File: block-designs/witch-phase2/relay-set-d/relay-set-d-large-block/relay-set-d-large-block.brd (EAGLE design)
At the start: 99.1 x 78.7 mm, 96 parts, among them IC1 74LVC1G06DBV, IC10 741G3157DBVR, IC11 741G3157DBVR, IC12 74LVC1G79DBV, IC13 74LVC1G79DBV, IC14 74LVC1G79DBV, IC15 74LVC1G79DBV, IC16 74LVC1G79DBV, IC17 74LVC1G08DBV, IC18 74LVC1G08DBV, IC19 74LVC1G08DBV, IC2 74LVC1G06DBV, IC20 74LVC1G08DBV, IC21 74LVC1G08DBV, IC22 74LVC1G08DBV, IC23 74LVC1G08DBV, IC24 74LVC1G08DBV, IC25 74LVC1G08DBV, IC26 74LVC1G08DBV, IC27 741G3157DBVR, IC28 741G3157DBVR, IC29 741G3157DBVR, IC3 74LVC1G06DBV, IC30 741G3157DBVR, IC31 741G3157DBVR, IC32 741G3157DBVR, IC33 741G3157DBVR, IC34 741G3157DBVR, IC35 741G3157DBVR, IC36 741G3157DBVR, IC37 74LVC1G32DBV, IC38 74LVC1G32DBV, IC39 74LVC1G32DBV, IC4 74LVC1G06DBV, IC40 74LVC1G32DBV, IC41 74LVC1G32DBV, IC42 74LVC1G32DBV, IC43 74LVC1G32DBV, IC44 74LVC1G32DBV, IC45 74LVC1G06DBV, IC46 74LVC1G06DBV, IC47 74LVC1G06DBV, IC48 74LVC1G06DBV, IC49 74LVC1G06DBV, IC5 74LVC1G06DBV, IC50 74LVC1G06DBV, IC51 74LVC1G06DBV, IC52 74LVC1G06DBV, IC53 74LVC1G06DBV, IC54 74LVC1G06DBV, IC55 74LVC1G06DBV, IC56 74LVC1G06DBV, IC6 741G3157DBVR, IC7 741G3157DBVR, IC8 741G3157DBVR, IC9 741G3157DBVR, Q1 MMBT2907ALT1SMD, Q2 MMBT2907ALT1SMD

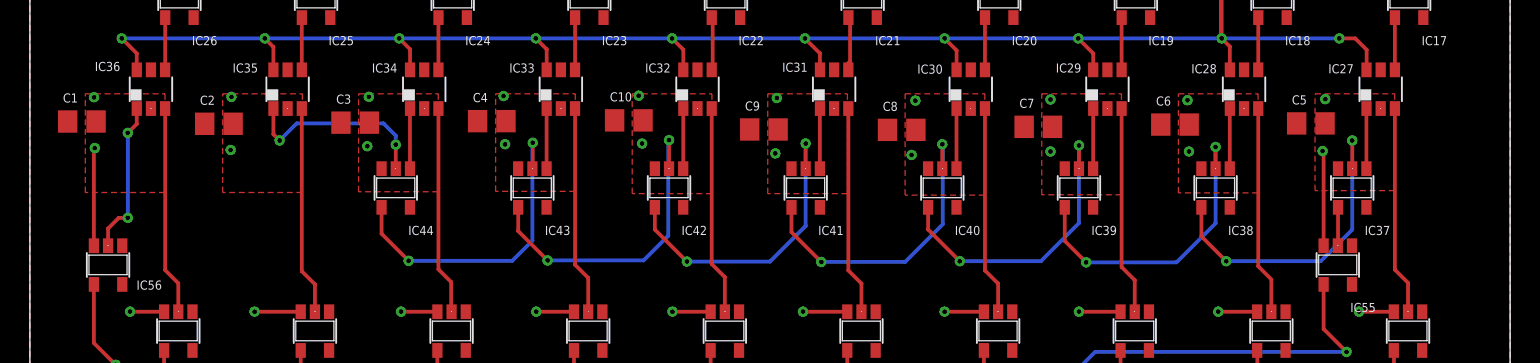
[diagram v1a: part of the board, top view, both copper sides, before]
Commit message: add pull down resistors to design
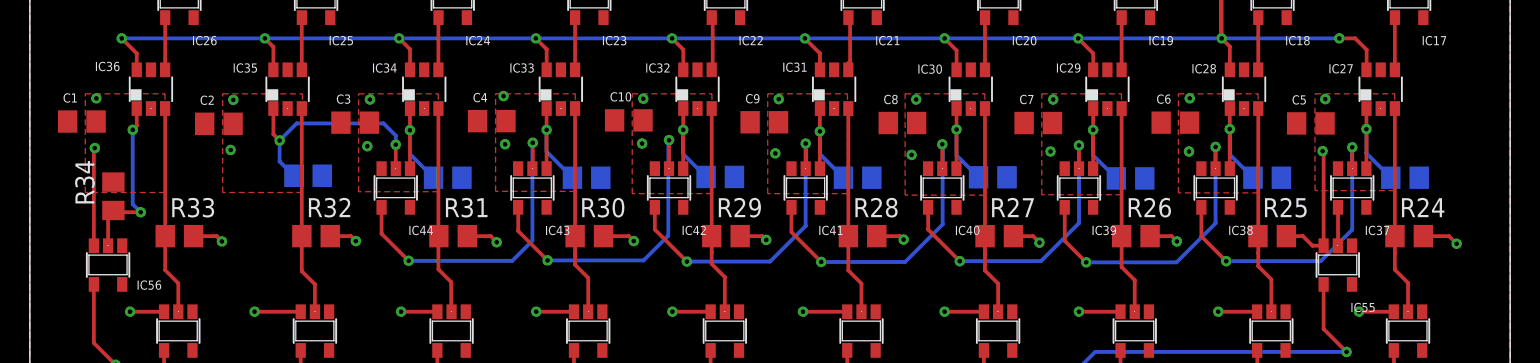
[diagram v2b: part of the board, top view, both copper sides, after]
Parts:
- added R15, R16, R17, R18, R19, R20, R21, R22, R23, R24, R25, R26, R27, R28, R29, R30, R31, R32, R33, R34: (no value), resistor:R0805
- moved C9 0.48 mm to (49.1, 28.6)
- moved C8 0.46 mm to (58.4, 28.5)
- moved C7 0.25 mm to (67.5, 28.5)
- moved C6 0.13 mm to (76.7, 28.5)
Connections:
- net EIGHT: now also R29.1
- net FIVE: now also R26.1
- net FOUR: now also R31.1
- net GND: now also R15.2, R16.2, R17.2, R18.2, R19.2, R20.2, R21.2, R22.2, R23.2, R24.2, R25.2, R26.2, R27.2, R28.2, R29.2, R30.2, R31.2, R32.2, R33.2, R34.2
- net N$10: now also R23.1
- net N$2: now also R15.1
- net N$3: now also R16.1
- net N$4: now also R17.1
- net N$5: now also R18.1
- net N$6: now also R19.1
- net N$7: now also R20.1
- net N$8: now also R21.1
- net N$9: now also R22.1
- net NINE: now also R24.1
- net ONE: now also R28.1
- net SEVEN: now also R25.1
- net SIX: now also R30.1
- net THREE: now also R27.1
- net TWO: now also R32.1
- net ZERO: now also R33.1
- net ZERO_OUT: now also R34.1
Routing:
- net GND: track 95.4 -> 116.5 mm, vias 58 -> 67
- net N$10: track 4.03 -> 7.95 mm, vias 0 -> 1
- net N$4: track 4.03 -> 7.94 mm, vias 0 -> 1
- net N$9: track 4.03 -> 7.92 mm, vias 0 -> 1
- net N$8: track 4.03 -> 7.92 mm, vias 0 -> 1
- net N$3: track 4.03 -> 7.86 mm, vias 0 -> 1
- net N$7: track 4.03 -> 7.84 mm, vias 0 -> 1
- net N$5: track 4.03 -> 7.81 mm, vias 0 -> 1
- net N$6: track 4.03 -> 7.78 mm, vias 0 -> 1
- net N$2: track 13.1 -> 15.9 mm
- net ZERO_OUT: track 10.3 -> 11.9 mm
- net N$17: track 21.5 -> 20.5 mm

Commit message: minor tweaks to original large block design
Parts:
- removed IC16: 74LVC1G79DBV, 74xx-little-us:SOT23-5
- removed R32, R33, R34: (no value), resistor:R0805
- added C16: (no value), resistor:C0805
- added IC57, IC59: 74LVC1G125DBV, 74xx-little-us:SOT23-5
- added IC58: 74LVC1G04DBV, 74xx-little-us:SOT23-5
- IC10, IC28, IC29, IC30, IC31, IC32, IC33, IC34, IC35, IC36, IC6, IC7, IC8, IC9: value 741G3157DBVR -> 74LVC1G125DBV; device 74xx-little-us:DBV_R-PDSO-G6 -> 74xx-little-us:SOT23-5
- IC11: value 741G3157DBVR -> 741G175
- IC12, IC13, IC14, IC15: value 74LVC1G79DBV -> 741G175; device 74xx-little-us:SOT23-5 -> 74xx-little-us:DBV_R-PDSO-G6
- IC27: value 741G3157DBVR -> 74LVC1G04DBV; device 74xx-little-us:DBV_R-PDSO-G6 -> 74xx-little-us:SOT23-5
- IC45, IC46, IC47, IC48, IC49, IC50, IC51, IC52, IC53, IC54, IC55: value 74LVC1G06DBV -> 74LVC1G04DBV
- IC56: value 74LVC1G06DBV -> 74LVC1G125DBV
- moved IC11 428.8 mm to (-334.2, -71.5), turned to 0 degrees
- moved IC15 417.3 mm to (-334.2, -100.7), turned to 0 degrees
- moved IC10 410.3 mm to (-333.6, -43.7), turned to 0 degrees
- moved IC14 406.1 mm to (-334.2, -93.4), turned to 0 degrees
- moved R27 405.9 mm to (-334.6, -51.0)
- moved R28 397.7 mm to (-334.6, -54.9)
- moved IC13 394.9 mm to (-334.2, -86.1), turned to 0 degrees
- moved IC9 393.8 mm to (-325.6, -43.7), turned to 0 degrees
- moved R29 389.5 mm to (-334.6, -58.9)
- moved IC12 383.7 mm to (-334.2, -78.8), turned to 0 degrees
- moved R30 381.4 mm to (-334.6, -62.9)
- moved IC8 377.4 mm to (-317.6, -43.7), turned to 0 degrees
- moved R24 375.9 mm to (-278.8, -39.0)
- moved R23 375.6 mm to (-278.8, -35.0), flipped to the top, turned to 0 degrees
- moved R25 375.4 mm to (-286.8, -43.0)
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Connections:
- removed net LATCH: IC11.4, IC12.1, IC13.1, IC14.1, IC15.1, IC16.1
- removed net N$10: IC27.1, IC37.1, R23.1
- removed net N$2: IC35.1, IC44.2, R15.1
- removed net N$3: IC34.1, IC44.1, R16.1
- removed net N$4: IC33.1, IC43.1, R17.1
- removed net N$5: IC32.1, IC42.1, R18.1
- removed net N$6: IC31.1, IC41.1, R19.1
- removed net N$7: IC30.1, IC40.1, R20.1
- removed net N$8: IC29.1, IC39.1, R21.1
- removed net N$9: IC28.1, IC38.1, R22.1
- removed net ZERO_OUT: IC36.1, IC56.2, R34.1
- new net AB_OUT0: IC56.2, IC57.2
- new net DSA-DSB_N: IC57.1, IC58.4, IC59.1
- new net OUT0: IC54.2, IC57.4, R25.1
- new net OUT1-9: IC55.2, IC59.4, R26.1
- net 1-9_OUT: now also IC59.2; no longer IC55.2
- net AB_OUT: no longer IC36.4
- net AB_OUT1: now also IC36.2, IC44.2; no longer IC35.4
- net AB_OUT2: now also IC35.2, IC44.1; no longer IC34.4
- net AB_OUT3: now also IC34.2, IC43.1; no longer IC33.4
- net AB_OUT4: now also IC33.2, IC42.1; no longer IC32.4
- net AB_OUT5: now also IC32.2, IC41.1; no longer IC31.4
- net AB_OUT6: now also IC31.2, IC40.1; no longer IC30.4
- net AB_OUT7: now also IC30.2, IC39.1; no longer IC29.4
- net AB_OUT8: now also IC29.2, IC38.1; no longer IC28.4
- net AB_OUT9: now also IC28.2, IC37.1; no longer IC27.4
- net DA: now also IC11.1, R27.1; no longer IC12.2
- net DA_IN: now also IC6.2; no longer IC6.3
- net DA_OUT: now also IC11.4; no longer IC12.4
- net DB: now also IC12.1, R28.1; no longer IC13.2
- net DB_IN: now also IC7.2; no longer IC7.3
- net DB_OUT: now also IC12.4; no longer IC13.4
- net DC: now also IC13.1, R29.1; no longer IC14.2
- net DC_IN: now also IC8.2; no longer IC8.3
- net DC_OUT: now also IC13.4; no longer IC14.4
- net DD: now also IC14.1, R30.1; no longer IC15.2
- net DD_IN: now also IC9.2; no longer IC9.3
- net DD_OUT: now also IC14.4; no longer IC15.4
- net DE: now also IC15.1, R31.1; no longer IC16.2
- net DE_IN: now also IC10.2; no longer IC10.3
- net DE_OUT: now also IC15.4; no longer IC16.4
- net DGA: now also IC10.1, IC6.1, IC7.1, IC8.1, IC9.1; no longer IC10.6, IC11.6, IC6.6, IC7.6, IC8.6, IC9.6
- net DSA-DSB: now also IC28.1, IC29.1, IC30.1, IC31.1, IC32.1, IC33.1, IC34.1, IC35.1, IC36.1, IC56.1, IC58.2; no longer IC27.6, IC28.6, IC29.6, IC30.6, IC31.6, IC32.6, IC33.6, IC34.6, IC35.6, IC36.6
- net EIGHT: now also IC29.4, IC45.2, R16.1; no longer IC32.3, IC50.2, R29.1
- net EIGHT_N: now also IC45.4, JP1.11; no longer IC50.4, JP1.7
- net FIVE: now also IC32.4, IC48.2, R19.1; no longer IC29.3, IC47.2, R26.1
- net FIVE_N: now also IC48.4, JP1.8; no longer IC47.4, JP1.10
- net FOUR: now also IC33.4, IC49.2, R20.1; no longer IC34.3, IC52.2, R31.1
- net FOUR_N: now also IC49.4, JP1.7; no longer IC52.4, JP1.5
- net GND: now also C16.2, IC10.3, IC12.2, IC13.2, IC14.2, IC15.2, IC27.3, IC28.3, IC29.3, IC30.3, IC31.3, IC32.3, IC33.3, IC34.3, IC35.3, IC36.3, IC57.3, IC58.3, IC59.3, IC6.3, IC7.3, IC8.3, IC9.3; no longer IC10.2, IC11.1, IC12.3, IC13.3, IC14.3, IC15.3, IC16.3, IC27.2, IC28.2, IC29.2, IC30.2, IC31.2, IC32.2, IC33.2, IC34.2, IC35.2, IC36.2, IC6.2, IC7.2, IC8.2, IC9.2, R32.2, R33.2, R34.2
- net NINE: now also IC27.2, IC28.4, R15.1; no longer IC27.3, IC45.2, R24.1
- net NINE_N: now also IC27.4; no longer IC45.4
- net ONE: now also IC36.4, IC52.2, R23.1; no longer IC31.3, IC49.2, R28.1
- net ONE_N: now also IC52.4, JP1.4; no longer IC49.4, JP1.8
- net RESET: now also IC11.6, IC12.6, IC13.6, IC14.6, IC15.6; no longer IC10.1, IC6.1, IC7.1, IC8.1, IC9.1
- net SEVEN: now also IC30.4, R17.1; no longer IC28.3, R25.1
- net SEVEN_N: now also JP1.10; no longer JP1.11
- net SIX: now also IC31.4, IC47.2, R18.1; no longer IC33.3, IC51.2, R30.1
- net SIX_N: now also IC47.4, JP1.9; no longer IC51.4, JP1.6
- net THREE: now also IC34.4, IC50.2, R21.1; no longer IC30.3, IC48.2, R27.1
- net THREE_N: now also IC50.4, JP1.6; no longer IC48.4, JP1.9
- net TWO: now also IC35.4, IC51.2, R22.1; no longer IC35.3, IC53.2, R32.1
- net TWO_N: now also IC51.4, JP1.5; no longer IC53.4, JP1.4
- net VCC: now also C16.1, IC12.3, IC13.3, IC14.3, IC15.3, IC57.5, IC58.5, IC59.5; no longer IC16.5
- net ZERO: now also IC53.2, IC56.4, R24.1; no longer IC36.3, IC54.2, R33.1
- net ZERO_N: now also IC53.4; no longer IC54.4
- net ZERO_OUT_N: now also IC54.4; no longer IC56.4
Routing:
- net DSA-DSB: track 172.8 -> 0.00 mm, vias 11 -> 0
- net DB_OUT: track 122.2 -> 0.00 mm, vias 5 -> 0
- net DA_OUT: track 121.0 -> 0.00 mm, vias 5 -> 0
- net GND: track 116.5 -> 0.00 mm, vias 67 -> 0
- net DGA: track 113.3 -> 0.00 mm, vias 6 -> 0
- net DC_OUT: track 100.0 -> 0.00 mm, vias 5 -> 0
- net DATA_N: track 98.9 -> 0.00 mm, vias 6 -> 0
- net DD_OUT: track 92.7 -> 0.00 mm, vias 5 -> 0
- net DE_OUT: track 87.6 -> 0.00 mm, vias 5 -> 0
- net RESET: track 68.4 -> 0.00 mm, vias 5 -> 0
- net LATCH: track 58.5 -> 0.00 mm, vias 6 -> 0
- net ZERO_OUT_N: track 42.1 -> 0.00 mm, vias 1 -> 0
- net NINE_N: track 38.2 -> 0.00 mm
- net ZERO_N: track 38.1 -> 0.00 mm
- net 1-9_OUT_N: track 36.5 -> 0.00 mm, vias 1 -> 0
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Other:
- board text added: "Relay Set D"
- board text removed: "Relay Set "D""
